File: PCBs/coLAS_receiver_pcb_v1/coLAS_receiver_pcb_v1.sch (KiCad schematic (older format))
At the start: 2 parts

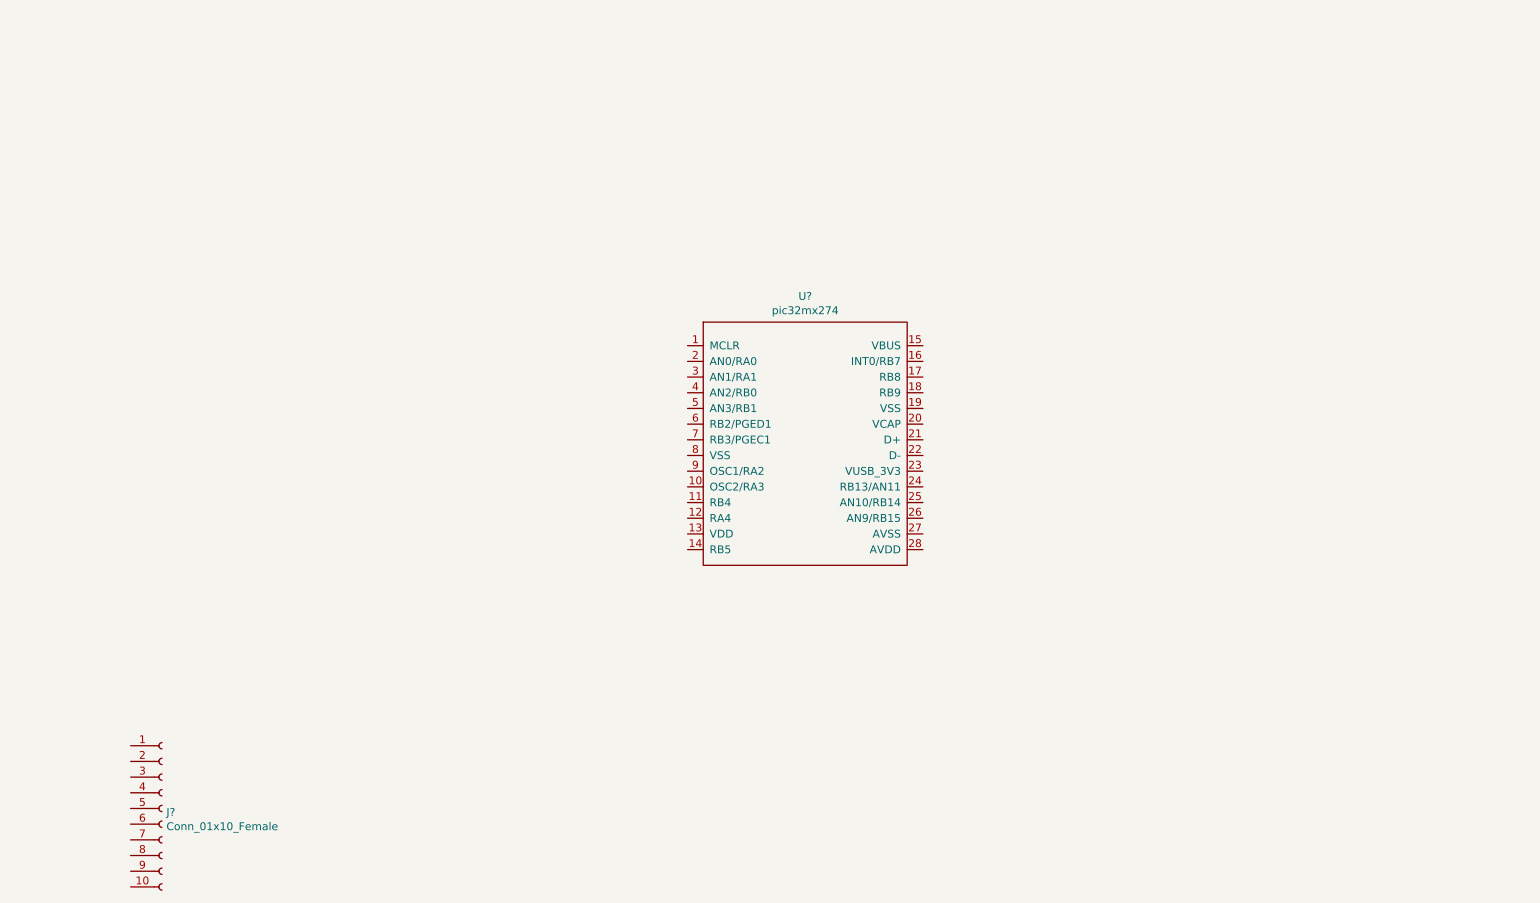
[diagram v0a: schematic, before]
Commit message: added op amps and ultrasonic trans to schematic
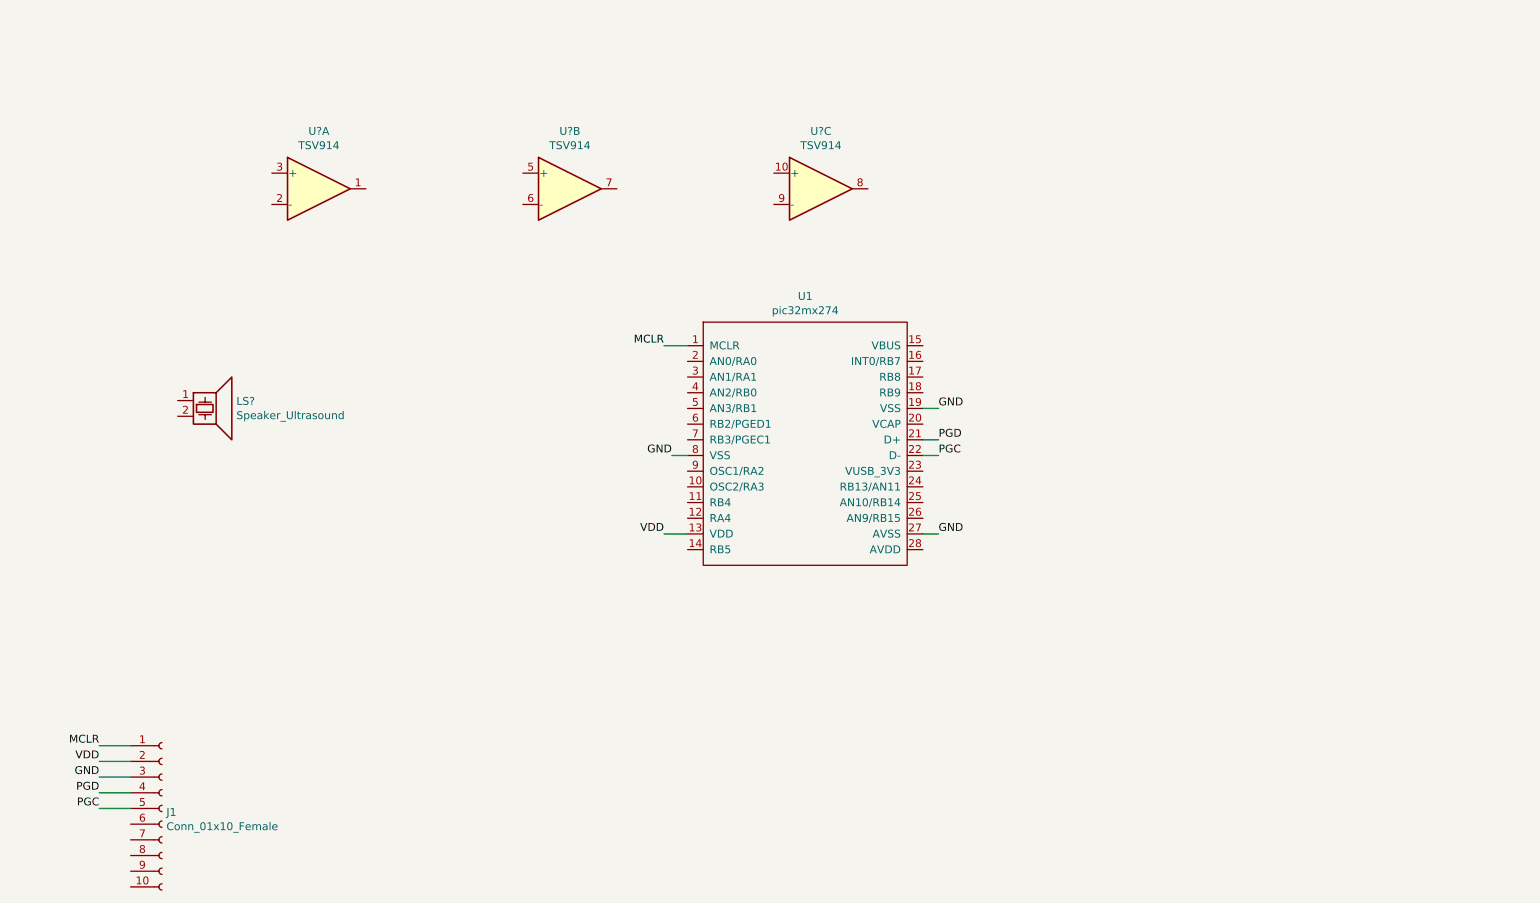
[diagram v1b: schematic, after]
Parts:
- added LS?: Speaker_Ultrasound, symbol Device:Speaker_Ultrasound
- added U? (x3): TSV914, symbol Amplifier_Operational:TSV914
- J1: renamed from J?; footprint (none) -> Connector_FFC-FPC:Hirose_FH12-10S-0.5SH_1x10-1MP_P0.50mm_Horizontal
- U1: renamed from U?; footprint (none) -> kicad_footprints:pic32mx274_soic28
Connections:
- net MCLR: now reaches U1.1 (MCLR)
- net MCLR: now also J1.1 (Pin_1)
- net VDD: now reaches U1.13 (VDD)
- net VDD: now also J1.2 (Pin_2)
- net GND: now reaches U1.19 (VSS)
- net GND: now also J1.3 (Pin_3), U1.27 (AVSS), U1.8 (VSS)
- net PGD: now reaches U1.21 (D+)
- net PGD: now also J1.4 (Pin_4)
- net PGC: now reaches U1.22 (D-)
- net PGC: now also J1.5 (Pin_5)
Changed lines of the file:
@@
 $EndDescr
 $Comp
-L Kicad_symbols:pic32mx274 U?
+L Kicad_symbols:pic32mx274 U1
 U 1 1 5E965B47
 P 5750 3200
-F 0 "U?" H 5950 3965 50  0000 C CNN
+F 0 "U1" H 5950 3965 50  0000 C CNN
 F 1 "pic32mx274" H 5950 3874 50  0000 C CNN
-F 2 "" H 6300 3200 50  0001 C CNN
+F 2 "kicad_footprints:pic32mx274_soic28" H 6300 3200 50  0001 C CNN
 F 3 "" H 6300 3200 50  0001 C CNN
 	1    5750 3200
@@
 $EndComp
 $Comp
-L Connector:Conn_01x10_Female J?
+L Connector:Conn_01x10_Female J1
 U 1 1 5E966E5E
 P 1850 5700
-F 0 "J?" H 1878 5676 50  0000 L CNN
+F 0 "J1" H 1878 5676 50  0000 L CNN
 F 1 "Conn_01x10_Female" H 1878 5585 50  0000 L CNN
-F 2 "" H 1850 5700 50  0001 C CNN
+F 2 "Connector_FFC-FPC:Hirose_FH12-10S-0.5SH_1x10-1MP_P0.50mm_Horizontal" H 1850 5700 50  0001 C CNN
 F 3 "~" H 1850 5700 50  0001 C CNN
 	1    1850 5700
 	1    0    0    -1
 $EndComp
+Text Label 1450 5300 2    50   ~ 0
+MCLR
+Text Label 1450 5400 2    50   ~ 0
+VDD
+Text Label 1450 5500 2    50   ~ 0
+GND
+Text Label 1450 5600 2    50   ~ 0
+PGD
+Text Label 1450 5700 2    50   ~ 0
+PGC
+Text Label 5050 2750 2    50   ~ 0
+MCLR
+Text Label 6800 3350 0    50   ~ 0
+PGD
+Text Label 6800 3450 0    50   ~ 0
+PGC
+Text Label 5050 3950 2    50   ~ 0
+VDD
+Text Label 6800 3150 0    50   ~ 0
+GND
+Text Label 5100 3450 2    50   ~ 0
+GND
+Text Label 6800 3950 0    50   ~ 0
+GND
+Wire Wire Line
+	5050 2750 5200 2750
+Wire Wire Line
+	5100 3450 5200 3450
+Wire Wire Line
+	5050 3950 5200 3950
+Wire Wire Line
+	6700 3950 6800 3950
+Wire Wire Line
+	6700 3450 6800 3450
+Wire Wire Line
+	6700 3350 6800 3350
+Wire Wire Line
+	6700 3150 6800 3150
+Wire Wire Line
+	1450 5300 1650 5300
+Wire Wire Line
+	1450 5400 1650 5400
+Wire Wire Line
+	1450 5500 1650 5500
+Wire Wire Line
+	1450 5600 1650 5600
+Wire Wire Line
+	1450 5700 1650 5700
+$Comp
+L Amplifier_Operational:TSV914 U?
+U 1 1 5E971669
+P 2850 1750
+F 0 "U?" H 2850 2117 50  0000 C CNN
+F 1 "TSV914" H 2850 2026 50  0000 C CNN
+F 2 "" H 2800 1850 50  0001 C CNN
+F 3 "www.st.com/resource/en/datasheet/tsv911.pdf" H 2900 1950 50  0001 C CNN
+	1    2850 1750
+	1    0    0    -1
+$EndComp
+$Comp
+L Amplifier_Operational:TSV914 U?
+U 2 1 5E976E00
+P 4450 1750
+F 0 "U?" H 4450 2117 50  0000 C CNN
+F 1 "TSV914" H 4450 2026 50  0000 C CNN
+F 2 "" H 4400 1850 50  0001 C CNN
+F 3 "www.st.com/resource/en/datasheet/tsv911.pdf" H 4500 1950 50  0001 C CNN
+	2    4450 1750
+	1    0    0    -1
+$EndComp
+$Comp
+L Amplifier_Operational:TSV914 U?
+U 3 1 5E978039
+P 6050 1750
+F 0 "U?" H 6050 2117 50  0000 C CNN
+F 1 "TSV914" H 6050 2026 50  0000 C CNN
+F 2 "" H 6000 1850 50  0001 C CNN
+F 3 "www.st.com/resource/en/datasheet/tsv911.pdf" H 6100 1950 50  0001 C CNN
+	3    6050 1750
+	1    0    0    -1
+$EndComp
+$Comp
+L Device:Speaker_Ultrasound LS?
+U 1 1 5E97938F
+P 2150 3100
+F 0 "LS?" H 2324 3096 50  0000 L CNN
+F 1 "Speaker_Ultrasound" H 2324 3005 50  0000 L CNN
+F 2 "" H 2115 3050 50  0001 C CNN
+F 3 "~" H 2115 3050 50  0001 C CNN
+	1    2150 3100
+	1    0    0    -1
+$EndComp

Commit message: FIXED PIC32MX274 SYMBOL ERRORS
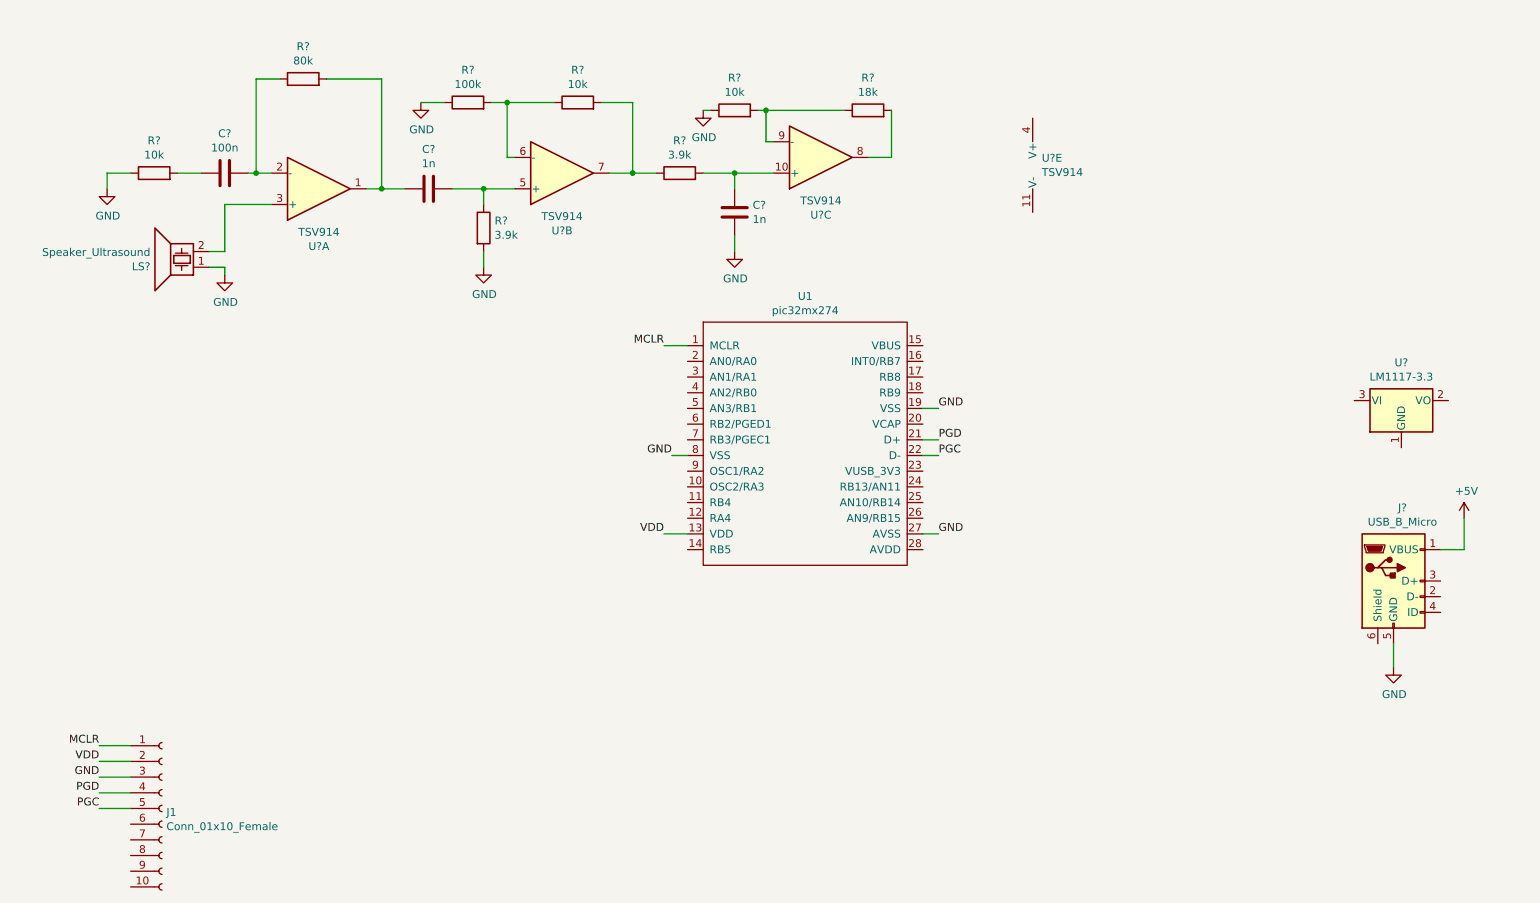
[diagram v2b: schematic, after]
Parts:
- added C?: 100n, symbol Device:C
- added C? (x2): 1n, symbol Device:C
- added J?: USB_B_Micro, symbol Connector:USB_B_Micro
- added R? (x3): 10k, symbol Device:R
- added R?: 80k, symbol Device:R
- added R?: 100k, symbol Device:R
- added R? (x2): 3.9k, symbol Device:R
- added R?: 18k, symbol Device:R
- added U?: TSV914, symbol Amplifier_Operational:TSV914
- added U?: LM1117-3.3, symbol Regulator_Linear:LM1117-3.3
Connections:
- net GND: now also LS?.1, C?.1, J?.5 (GND), R?.1, R?.1, R?.1, R?.2
- net at U?.1: now also C?.2, R?.2
- net at U?.2 (-): now also C?.1, R?.1
- net at U?.3 (+): now also LS?.2
- net at U?.5 (+): now also C?.1, R?.1
- net at U?.6 (-): now also R?.1, R?.2
- net at U?.7: now also R?.1, R?.2
- net at U?.10 (+): now also C?.2, R?.2
- net at U?.8: now also R?.2
- net at U?.9 (-): now also R?.1, R?.2
- new net: C?.2, R?.2
- new net +5V: J?.1 (VBUS)
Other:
- moved on the sheet: LS?, U?B, U?C

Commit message: schematic progress
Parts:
- added C?: .1uF, symbol Device:C
- added C?: 1uF, symbol Device:C
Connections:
- net +5V: now also U1.15 (VBUS), U?.3 (VI), C?.1
- net GND: now also U?.1 (GND), C?.2, C?.2
- net PGC: now also U1.7 (RB3/PGEC1); no longer U1.22 (D-)
- net PGD: now also U1.6 (RB2/PGED1); no longer U1.21 (D+)
- net +3V3: now reaches U?.2 (VO)
- net +3V3: now also C?.1
- net D-: now reaches J?.2 (D-)
- net D+: now reaches J?.3 (D+)
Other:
- moved on the sheet: U?
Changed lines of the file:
@@
 Text Label 5050 2750 2    50   ~ 0
 MCLR
-Text Label 6800 3350 0    50   ~ 0
+Text Label 5100 3250 2    50   ~ 0
 PGD
-Text Label 6800 3450 0    50   ~ 0
+Text Label 5100 3350 2    50   ~ 0
 PGC
 Text Label 5050 3950 2    50   ~ 0
@@
 	6700 3950 6800 3950
 Wire Wire Line
-	6700 3450 6800 3450
-Wire Wire Line
-	6700 3350 6800 3350
-Wire Wire Line
 	6700 3150 6800 3150
 Wire Wire Line
@@
 L Regulator_Linear:LM1117-3.3 U?
 U 1 1 5E9D8507
-P 9750 3100
-F 0 "U?" H 9750 3342 50  0000 C CNN
-F 1 "LM1117-3.3" H 9750 3251 50  0000 C CNN
-F 2 "" H 9750 3100 50  0001 C CNN
-F 3 "http://www.ti.com/lit/ds/symlink/lm1117.pdf" H 9750 3100 50  0001 C CNN
-	1    9750 3100
+P 9750 2500
+F 0 "U?" H 9750 2742 50  0000 C CNN
+F 1 "LM1117-3.3" H 9750 2651 50  0000 C CNN
+F 2 "" H 9750 2500 50  0001 C CNN
+F 3 "http://www.ti.com/lit/ds/symlink/lm1117.pdf" H 9750 2500 50  0001 C CNN
+	1    9750 2500
 	1    0    0    -1
 $EndComp
@@
 Wire Wire Line
 	9700 4650 9700 4800
+Text Label 10100 4250 0    50   ~ 0
+D+
+Text Label 10100 4350 0    50   ~ 0
+D-
+Wire Wire Line
+	10000 4250 10100 4250
+Wire Wire Line
+	10000 4350 10100 4350
+$Comp
+L power:GND #PWR?
+U 1 1 5EA22415
+P 9750 3000
+F 0 "#PWR?" H 9750 2750 50  0001 C CNN
+F 1 "GND" H 9755 2827 50  0000 C CNN
+F 2 "" H 9750 3000 50  0001 C CNN
+F 3 "" H 9750 3000 50  0001 C CNN
+	1    9750 3000
+	1    0    0    -1
+$EndComp
+Wire Wire Line
+	9750 2800 9750 2900
+$Comp
+L power:+5V #PWR?
+U 1 1 5EA23B8F
+P 9100 2400
+F 0 "#PWR?" H 9100 2250 50  0001 C CNN
+F 1 "+5V" H 9115 2573 50  0000 C CNN
+F 2 "" H 9100 2400 50  0001 C CNN
+F 3 "" H 9100 2400 50  0001 C CNN
+	1    9100 2400
+	1    0    0    -1
+$EndComp
+Wire Wire Line
+	9100 2400 9100 2500
+Wire Wire Line
+	9100 2500 9250 2500
+$Comp
+L power:+3.3V #PWR?
+U 1 1 5EA25532
+P 10400 2350
+F 0 "#PWR?" H 10400 2200 50  0001 C CNN
+F 1 "+3.3V" H 10415 2523 50  0000 C CNN
+F 2 "" H 10400 2350 50  0001 C CNN
+F 3 "" H 10400 2350 50  0001 C CNN
+	1    10400 2350
+	1    0    0    -1
+$EndComp
+Wire Wire Line
+	10050 2500 10250 2500
+Wire Wire Line
+	10400 2500 10400 2350
+$Comp
+L Device:C C?
+U 1 1 5EA29440
+P 9250 2750
+F 0 "C?" H 9365 2796 50  0000 L CNN
+F 1 ".1uF" H 9365 2705 50  0000 L CNN
+F 2 "" H 9288 2600 50  0001 C CNN
+F 3 "~" H 9250 2750 50  0001 C CNN
+	1    9250 2750
+	1    0    0    -1
+$EndComp
+$Comp
+L Device:C C?
+U 1 1 5EA298B3
+P 10250 2750
+F 0 "C?" H 10365 2796 50  0000 L CNN
+F 1 "1uF" H 10365 2705 50  0000 L CNN
+F 2 "" H 10288 2600 50  0001 C CNN
+F 3 "~" H 10250 2750 50  0001 C CNN
+	1    10250 2750
+	1    0    0    -1
+$EndComp
+Wire Wire Line
+	9250 2500 9250 2600
+Connection ~ 9250 2500
+Wire Wire Line
+	9250 2500 9450 2500
+Wire Wire Line
+	9250 2900 9750 2900
+Connection ~ 9750 2900
+Wire Wire Line
+	9750 2900 9750 3000
+Wire Wire Line
+	10250 2500 10250 2600
+Connection ~ 10250 2500
+Wire Wire Line
+	10250 2500 10400 2500
+Wire Wire Line
+	10250 2900 9750 2900
+Wire Wire Line
+	5100 3250 5200 3250
+Wire Wire Line
+	5100 3350 5200 3350
+$Comp
+L power:+5V #PWR?
+U 1 1 5EA36903
+P 6850 2650
+F 0 "#PWR?" H 6850 2500 50  0001 C CNN
+F 1 "+5V" H 6865 2823 50  0000 C CNN
+F 2 "" H 6850 2650 50  0001 C CNN
+F 3 "" H 6850 2650 50  0001 C CNN
+	1    6850 2650
+	1    0    0    -1
+$EndComp
+Wire Wire Line
+	6700 2750 6850 2750
+Wire Wire Line
+	6850 2750 6850 2650
 $EndSCHEMATC

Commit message: added comporator to kicad schem
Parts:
- added R?: 1Meg, symbol Device:R_Small
- added R?: 15k, symbol Device:R_Small
- added U?: TSV914, symbol Amplifier_Operational:TSV914
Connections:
- net +3V3: now also U?.4 (V+), R?.1
- net GND: now also U?.11 (V-), R?.2
- net U2_RX: now reaches U1.14 (RB5)
- net INT0: now reaches U1.16 (INT0/RB7)
- net INT0: now also U?.14
- net at R?.2, U?.8: now also U?.12 (+)
- new net: R?.1, R?.2, U?.13 (-)
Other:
- moved on the sheet: U?E
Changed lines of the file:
@@
 L Amplifier_Operational:TSV914 U?
 U 5 1 5E9D07ED
-P 7500 1600
-F 0 "U?" H 7458 1646 50  0000 L CNN
-F 1 "TSV914" H 7458 1555 50  0000 L CNN
-F 2 "" H 7450 1700 50  0001 C CNN
-F 3 "www.st.com/resource/en/datasheet/tsv911.pdf" H 7550 1800 50  0001 C CNN
-	5    7500 1600
+P 9100 1250
+F 0 "U?" H 9058 1296 50  0000 L CNN
+F 1 "TSV914" H 9058 1205 50  0000 L CNN
+F 2 "" H 9050 1350 50  0001 C CNN
+F 3 "www.st.com/resource/en/datasheet/tsv911.pdf" H 9150 1450 50  0001 C CNN
+	5    9100 1250
 	1    0    0    -1
 $EndComp
@@
 Wire Wire Line
 	6850 2750 6850 2650
+$Comp
+L Amplifier_Operational:TSV914 U?
+U 4 1 5E9B4BF7
+P 7650 1450
+F 0 "U?" H 7650 1083 50  0000 C CNN
+F 1 "TSV914" H 7650 1174 50  0000 C CNN
+F 2 "" H 7600 1550 50  0001 C CNN
+F 3 "www.st.com/resource/en/datasheet/tsv911.pdf" H 7700 1650 50  0001 C CNN
+	4    7650 1450
+	1    0    0    1
+$EndComp
+Wire Wire Line
+	6500 1550 7350 1550
+Connection ~ 6500 1550
+$Comp
+L Device:R_Small R?
+U 1 1 5E9D0AB4
+P 7400 950
+F 0 "R?" V 7204 950 50  0000 C CNN
+F 1 "1Meg" V 7295 950 50  0000 C CNN
+F 2 "" H 7400 950 50  0001 C CNN
+F 3 "~" H 7400 950 50  0001 C CNN
+	1    7400 950
+	0    1    1    0
+$EndComp
+$Comp
+L Device:R_Small R?
+U 1 1 5E9D233F
+P 7050 950
+F 0 "R?" V 6854 950 50  0000 C CNN
+F 1 "15k" V 6945 950 50  0000 C CNN
+F 2 "" H 7050 950 50  0001 C CNN
+F 3 "~" H 7050 950 50  0001 C CNN
+	1    7050 950
+	0    1    1    0
+$EndComp
+$Comp
+L power:GND #PWR?
+U 1 1 5E9D26D4
+P 6800 1000
+F 0 "#PWR?" H 6800 750 50  0001 C CNN
+F 1 "GND" H 6805 827 50  0000 C CNN
+F 2 "" H 6800 1000 50  0001 C CNN
+F 3 "" H 6800 1000 50  0001 C CNN
+	1    6800 1000
+	1    0    0    -1
+$EndComp
+Wire Wire Line
+	6800 1000 6800 950
+Wire Wire Line
+	6800 950  6950 950
+Wire Wire Line
+	7150 950  7250 950
+$Comp
+L power:+3.3V #PWR?
+U 1 1 5E9D6545
+P 7700 900
+F 0 "#PWR?" H 7700 750 50  0001 C CNN
+F 1 "+3.3V" H 7715 1073 50  0000 C CNN
+F 2 "" H 7700 900 50  0001 C CNN
+F 3 "" H 7700 900 50  0001 C CNN
+	1    7700 900
+	1    0    0    -1
+$EndComp
+Wire Wire Line
+	7500 950  7700 950
+Wire Wire Line
+	7700 950  7700 900
+Wire Wire Line
+	7250 950  7250 1350
+Wire Wire Line
+	7250 1350 7350 1350
+Connection ~ 7250 950
+Wire Wire Line
+	7250 950  7300 950
+Text Label 8200 1450 0    50   ~ 0
+INT0
+Wire Wire Line
+	7950 1450 8200 1450
+Text Label 6800 2850 0    50   ~ 0
+INT0
+Wire Wire Line
+	6700 2850 6800 2850
+$Comp
+L power:GND #PWR?
+U 1 1 5E9F2463
+P 9000 1650
+F 0 "#PWR?" H 9000 1400 50  0001 C CNN
+F 1 "GND" H 9005 1477 50  0000 C CNN
+F 2 "" H 9000 1650 50  0001 C CNN
+F 3 "" H 9000 1650 50  0001 C CNN
+	1    9000 1650
+	1    0    0    -1
+$EndComp
+$Comp
+L power:+3.3V #PWR?
+U 1 1 5E9F2A48
+P 9000 850
+F 0 "#PWR?" H 9000 700 50  0001 C CNN
+F 1 "+3.3V" H 9015 1023 50  0000 C CNN
+F 2 "" H 9000 850 50  0001 C CNN
+F 3 "" H 9000 850 50  0001 C CNN
+	1    9000 850
+	1    0    0    -1
+$EndComp
+Wire Wire Line
+	9000 1650 9000 1550
+Wire Wire Line
+	9000 850  9000 950
+Text Label 5050 4050 2    50   ~ 0
+U2_RX
+Wire Wire Line
+	5050 4050 5200 4050
 $EndSCHEMATC

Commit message: began assigning footprints
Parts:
- added U2: TSOP6238TT, symbol Kicad_symbols:TSOP6238TT
- C1, C2, C3, C4, C5: renamed from C?; footprint (none) -> Capacitor_SMD:C_0805_2012Metric_Pad1.15x1.40mm_HandSolder
- J2: renamed from J?; footprint (none) -> Connector_USB:USB_Micro-B_Molex-105017-0001
- R1, R10, R2, R3, R4, R5, R6, R7, R8, R9: renamed from R?; footprint (none) -> Resistor_SMD:R_0805_2012Metric_Pad1.15x1.40mm_HandSolder
- U4: renamed from U?; footprint (none) -> Package_TO_SOT_SMD:SOT-223
- gave numbers to parts that had none: 2
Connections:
- net +3V3: now also U2.3 (Vs)
- net GND: now also U2.1 (GND)
- net U2_RX: now also U2.4 (OUT)
